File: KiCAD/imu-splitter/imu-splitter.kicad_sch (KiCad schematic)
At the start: 11 parts, among them J1 4P4C, J2 4P4C, J3 4P4C, J4 4P4C, J5 4P4C, J6 4P4C, J7 SHF-113-01-L-D-SM, J8 Conn_01x04, U1 AZ1117-3.3

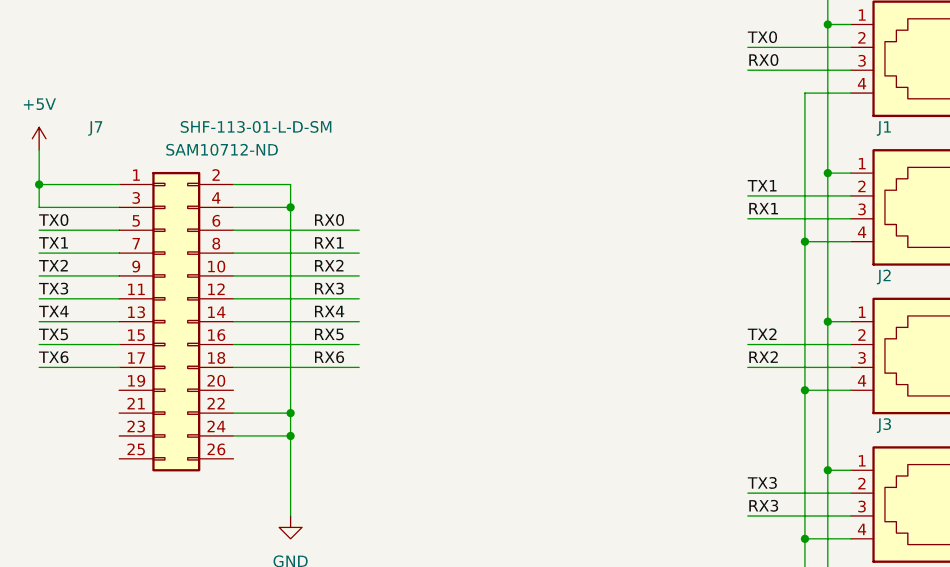
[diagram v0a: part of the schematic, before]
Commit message: tentative placement of splitter
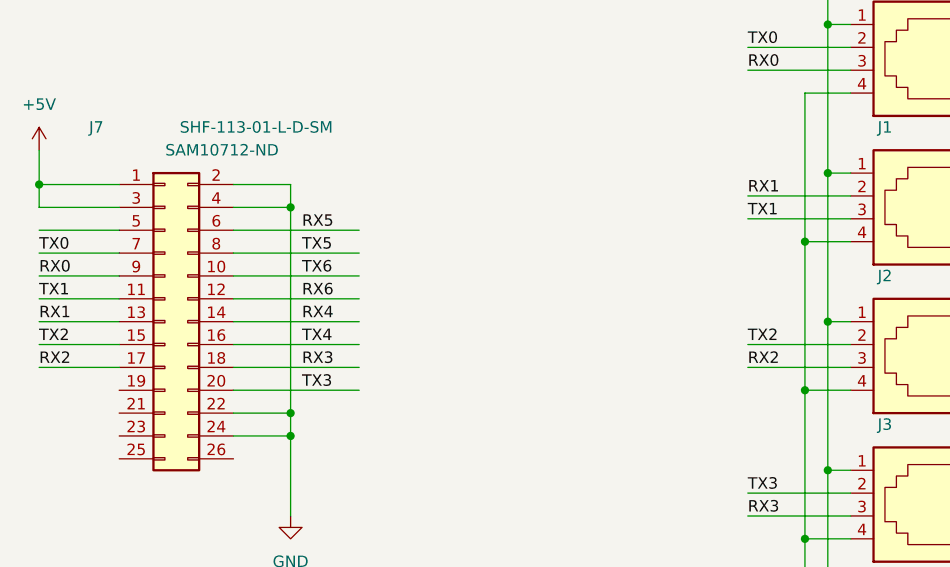
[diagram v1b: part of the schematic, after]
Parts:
- J7: footprint models:SAMTEC_SHF-113-01-L-D-SM -> models:SAMTEC_SHF-113-01-L-D-RA
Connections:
- net RX0: now also J7.9 (Pin_9); no longer J7.6 (Pin_6)
- net RX1: now also J2.2, J7.13 (Pin_13); no longer J2.3, J7.8 (Pin_8)
- net RX2: now also J7.17 (Pin_17); no longer J7.10 (Pin_10)
- net RX3: now also J7.18 (Pin_18); no longer J7.12 (Pin_12)
- net RX5: now also J7.6 (Pin_6); no longer J7.16 (Pin_16)
- net RX6: now also J7.12 (Pin_12); no longer J7.18 (Pin_18)
- net TX0: now also J7.7 (Pin_7); no longer J7.5 (Pin_5)
- net TX1: now also J2.3, J7.11 (Pin_11); no longer J2.2, J7.7 (Pin_7)
- net TX2: now also J7.15 (Pin_15); no longer J7.9 (Pin_9)
- net TX3: now also J7.20 (Pin_20); no longer J7.11 (Pin_11)
- net TX4: now also J7.16 (Pin_16); no longer J7.13 (Pin_13)
- net TX5: now also J7.8 (Pin_8); no longer J7.15 (Pin_15)
- net TX6: now also J7.10 (Pin_10); no longer J7.17 (Pin_17)
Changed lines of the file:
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@@
+    (stroke (width 0) (type default))
+  )
+  (wire (pts (xy 57.15 101.6) (xy 71.12 101.6))
     (stroke (width 0) (type default))
   )
@@
     (stroke (width 0) (type default))
   )
+  (wire (pts (xy 57.15 96.52) (xy 71.12 96.52))
+    (stroke (width 0) (type default))
+  )
   (wire (pts (xy 35.56 96.52) (xy 44.45 96.52))
     (stroke (width 0) (type default))
@@
     (stroke (width 0) (type default))
   )
-  (wire (pts (xy 57.15 96.52) (xy 71.12 96.52))
-    (stroke (width 0) (type default))
-  )
   (wire (pts (xy 57.15 88.9) (xy 71.12 88.9))
     (stroke (width 0) (type default))
@@
     (stroke (width 0) (type default))
   )
-  (label "TX2" (at 35.56 88.9 0) (fields_autoplaced)
+  (label "TX2" (at 35.56 96.52 0) (fields_autoplaced)
     (effects (font (size 1.27 1.27)) (justify left bottom))
   )
@@
     (effects (font (size 1.27 1.27)) (justify left bottom))
   )
-  (label "RX6" (at 66.04 99.06 0) (fields_autoplaced)
-    (effects (font (size 1.27 1.27)) (justify left bottom))
-  )
-  (label "TX1" (at 114.3 80.01 0) (fields_autoplaced)
-    (effects (font (size 1.27 1.27)) (justify left bottom))
-  )
-  (label "TX1" (at 35.56 86.36 0) (fields_autoplaced)
+  (label "TX5" (at 114.3 146.05 0) (fields_autoplaced)
+    (effects (font (size 1.27 1.27)) (justify left bottom))
+  )
+  (label "RX6" (at 64.77 91.44 0) (fields_autoplaced)
+    (effects (font (size 1.27 1.27)) (justify left bottom))
+  )
+  (label "TX1" (at 114.3 82.55 0) (fields_autoplaced)
+    (effects (font (size 1.27 1.27)) (justify left bottom))
+  )
+  (label "TX1" (at 35.56 91.44 0) (fields_autoplaced)
     (effects (font (size 1.27 1.27)) (justify left bottom))
   )
@@
     (effects (font (size 1.27 1.27)) (justify left bottom))
   )
-  (label "TX5" (at 114.3 146.05 0) (fields_autoplaced)
-    (effects (font (size 1.27 1.27)) (justify left bottom))
-  )
-  (label "TX3" (at 35.56 91.44 0) (fields_autoplaced)
-    (effects (font (size 1.27 1.27)) (justify left bottom))
-  )
-  (label "TX4" (at 35.56 93.98 0) (fields_autoplaced)
+  (label "TX5" (at 64.77 86.36 0) (fields_autoplaced)
+    (effects (font (size 1.27 1.27)) (justify left bottom))
+  )
+  (label "TX3" (at 64.77 101.6 0) (fields_autoplaced)
+    (effects (font (size 1.27 1.27)) (justify left bottom))
+  )
+  (label "TX4" (at 64.77 96.52 0) (fields_autoplaced)
     (effects (font (size 1.27 1.27)) (justify left bottom))
   )
@@
     (effects (font (size 1.27 1.27)) (justify left bottom))
   )
-  (label "RX3" (at 66.04 91.44 0) (fields_autoplaced)
-    (effects (font (size 1.27 1.27)) (justify left bottom))
-  )
-  (label "TX0" (at 35.56 83.82 0) (fields_autoplaced)
-    (effects (font (size 1.27 1.27)) (justify left bottom))
-  )
-  (label "RX5" (at 66.04 96.52 0) (fields_autoplaced)
+  (label "RX3" (at 64.77 99.06 0) (fields_autoplaced)
+    (effects (font (size 1.27 1.27)) (justify left bottom))
+  )
+  (label "TX0" (at 35.56 86.36 0) (fields_autoplaced)
+    (effects (font (size 1.27 1.27)) (justify left bottom))
+  )
+  (label "RX5" (at 64.77 83.82 0) (fields_autoplaced)
     (effects (font (size 1.27 1.27)) (justify left bottom))
   )
@@
     (effects (font (size 1.27 1.27)) (justify left bottom))
   )
-  (label "RX0" (at 66.04 83.82 0) (fields_autoplaced)
-    (effects (font (size 1.27 1.27)) (justify left bottom))
-  )
-  (label "RX1" (at 66.04 86.36 0) (fields_autoplaced)
+  (label "RX0" (at 35.56 88.9 0) (fields_autoplaced)
+    (effects (font (size 1.27 1.27)) (justify left bottom))
+  )
+  (label "RX1" (at 35.56 93.98 0) (fields_autoplaced)
     (effects (font (size 1.27 1.27)) (justify left bottom))
   )
@@
     (effects (font (size 1.27 1.27)) (justify left bottom))
   )
-  (label "RX2" (at 66.04 88.9 0) (fields_autoplaced)
+  (label "RX2" (at 35.56 99.06 0) (fields_autoplaced)
     (effects (font (size 1.27 1.27)) (justify left bottom))
   )
@@
     (effects (font (size 1.27 1.27)) (justify left bottom))
   )
-  (label "TX6" (at 35.56 99.06 0) (fields_autoplaced)
-    (effects (font (size 1.27 1.27)) (justify left bottom))
-  )
-  (label "RX1" (at 114.3 82.55 0) (fields_autoplaced)
+  (label "TX6" (at 64.77 88.9 0) (fields_autoplaced)
+    (effects (font (size 1.27 1.27)) (justify left bottom))
+  )
+  (label "RX1" (at 114.3 80.01 0) (fields_autoplaced)
     (effects (font (size 1.27 1.27)) (justify left bottom))
   )
@@
     (effects (font (size 1.27 1.27)) (justify left bottom))
   )
-  (label "TX5" (at 35.56 96.52 0) (fields_autoplaced)
-    (effects (font (size 1.27 1.27)) (justify left bottom))
-  )
-  (label "RX4" (at 66.04 93.98 0) (fields_autoplaced)
+  (label "RX4" (at 64.77 93.98 0) (fields_autoplaced)
     (effects (font (size 1.27 1.27)) (justify left bottom))
   )
@@
       (effects (font (size 1.27 1.27)))
     )
-    (property "Footprint" "models:SAMTEC_SHF-113-01-L-D-SM" (at 49.53 93.98 0)
-      (effects (font (size 1.27 1.27)) hide)
-    )
+    (property "Footprint" "models:SAMTEC_SHF-113-01-L-D-RA" (at 49.53 93.98 0)
+      (effects (font (size 1.27 1.27)) hide)
+    )

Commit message: updates before v1 fab
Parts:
- added D1, D2: LED, LED_SMD:LED_0805_2012Metric_Pad1.15x1.40mm_HandSolder, symbol Device:LED
- added J9: Conn_01x05, Connector_PinHeader_2.54mm:PinHeader_1x05_P2.54mm_Vertical, symbol Connector_Generic:Conn_01x05
- added R1: 1.5k, Resistor_SMD:R_0805_2012Metric_Pad1.20x1.40mm_HandSolder, symbol Device:R_US
- added R2: 510, Capacitor_SMD:C_0805_2012Metric_Pad1.18x1.45mm_HandSolder, symbol Device:R_US
- C1, C2: footprint Capacitor_SMD:C_0805_2012Metric -> Capacitor_SMD:C_0805_2012Metric_Pad1.18x1.45mm_HandSolder
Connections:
- net +3.3V: now also J9.2 (Pin_2), R2.1
- net +5V: now also J9.1 (Pin_1), R1.1
- net GND: now also D1.1 (K), D2.1 (K), J9.5 (Pin_5)
- net RX0: now also J7.14 (Pin_14), J9.4 (Pin_4); no longer J7.9 (Pin_9)
- net RX1: now also J7.12 (Pin_12); no longer J7.13 (Pin_13)
- net RX2: now also J7.6 (Pin_6); no longer J7.17 (Pin_17)
- net RX3: now also J7.9 (Pin_9); no longer J7.18 (Pin_18)
- net RX4: now also J7.17 (Pin_17); no longer J7.14 (Pin_14)
- net RX5: now also J7.21 (Pin_21); no longer J7.6 (Pin_6)
- net RX6: now also J7.11 (Pin_11); no longer J7.12 (Pin_12)
- net TX0: now also J7.16 (Pin_16), J9.3 (Pin_3); no longer J7.7 (Pin_7)
- net TX1: now also J7.10 (Pin_10); no longer J7.11 (Pin_11)
- net TX2: now also J7.8 (Pin_8); no longer J7.15 (Pin_15)
- net TX3: now also J7.7 (Pin_7); no longer J7.20 (Pin_20)
- net TX4: now also J7.15 (Pin_15); no longer J7.16 (Pin_16)
- net TX5: now also J7.19 (Pin_19); no longer J7.8 (Pin_8)
- net TX6: now also J7.13 (Pin_13); no longer J7.10 (Pin_10)
- new net: D1.2 (A), R1.2
- new net: D2.2 (A), R2.2
- no-connect marks 0 -> 3
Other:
- note added: "Test Point"
- moved on the sheet: C2

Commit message: Update KiCAD, start software
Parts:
- C1: CatNo (none) -> 1276-1096-1-ND; MfgNo (none) -> CL21A106KOQNNNE
- C2: CatNo (none) -> 1276-6526-1-ND; MfgNo (none) -> CL21A226KOQNNNE
- D1, D2: CatNo (none) -> 350-5973006607FCT-ND; MfgNo (none) -> 5973006607F
- J1, J2, J3, J4, J5, J6: CatNo (none) -> AE10381-ND; MfgNo (none) -> A-2004-3-4-LP-N-R
- J7: MfgNo (none) -> SHF-113-01-L-D-SM
- J8: CatNo (none) -> SAM10242-ND; MfgNo (none) -> TMS-104-01-G-S
- J9: CatNo (none) -> 609-3462-ND; MfgNo (none) -> 68000-105HLF
- R1: CatNo (none) -> 311-1.50KCRCT-ND; MfgNo (none) -> RC0805FR-071K5L
- R2: CatNo (none) -> 311-510CRCT-ND; MfgNo (none) -> RC0805FR-07510RL
- U1: MfgNo (none) -> AZ1117CH2-3.3TRG1
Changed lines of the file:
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@@
+      (effects (font (size 1.27 1.27)) hide)
+    )
+    (property "CatNo" "AE10381-ND" (at 135.89 80.01 0)
+      (effects (font (size 1.27 1.27)) hide)
+    )
+    (property "MfgNo" "A-2004-3-4-LP-N-R" (at 135.89 80.01 0)
       (effects (font (size 1.27 1.27)) hide)
     )
@@
       (effects (font (size 1.27 1.27)) hide)
     )
+    (property "CatNo" "1276-1096-1-ND" (at 62.23 45.72 0)
+      (effects (font (size 1.27 1.27)) hide)
+    )
+    (property "MfgNo" "CL21A106KOQNNNE" (at 62.23 45.72 0)
+      (effects (font (size 1.27 1.27)) hide)
+    )
     (pin "2")
     (pin "1")
@@
       (effects (font (size 1.27 1.27)) hide)
     )
+    (property "CatNo" "350-5973006607FCT-ND" (at 53.34 49.53 0)
+      (effects (font (size 1.27 1.27)) hide)
+    )
+    (property "MfgNo" "5973006607F" (at 53.34 49.53 0)
+      (effects (font (size 1.27 1.27)) hide)
+    )
     (pin "2")
     (pin "1")
@@
     )
     (property "Datasheet" "~" (at 53.34 39.37 0)
+      (effects (font (size 1.27 1.27)) hide)
+    )
+    (property "MfgNo" "RC0805FR-071K5L" (at 53.34 39.37 0)
+      (effects (font (size 1.27 1.27)) hide)
+    )
+    (property "CatNo" "311-1.50KCRCT-ND" (at 53.34 39.37 0)
       (effects (font (size 1.27 1.27)) hide)
     )
@@
       (effects (font (size 1.27 1.27)) hide)
     )
+    (property "CatNo" "AE10381-ND" (at 135.89 96.52 0)
+      (effects (font (size 1.27 1.27)) hide)
+    )
+    (property "MfgNo" "A-2004-3-4-LP-N-R" (at 135.89 96.52 0)
+      (effects (font (size 1.27 1.27)) hide)
+    )
     (pin "1")
     (pin "2")
@@
     )
     (property "Datasheet" "~" (at 67.31 144.78 0)
+      (effects (font (size 1.27 1.27)) hide)
+    )
+    (property "MfgNo" "68000-105HLF" (at 67.31 144.78 0)
+      (effects (font (size 1.27 1.27)) hide)
+    )
+    (property "CatNo" "609-3462-ND" (at 67.31 144.78 0)
       (effects (font (size 1.27 1.27)) hide)
     )
@@
     (property "CatNo" "SAM10712-ND" (at 55.88 74.93 0)
       (effects (font (size 1.27 1.27)))
+    )
+    (property "MfgNo" "SHF-113-01-L-D-SM" (at 49.53 93.98 0)
+      (effects (font (size 1.27 1.27)) hide)
     )
     (pin "5")
@@
       (effects (font (size 1.27 1.27)) hide)
     )
+    (property "CatNo" "AE10381-ND" (at 135.89 146.05 0)
+      (effects (font (size 1.27 1.27)) hide)
+    )
+    (property "MfgNo" "A-2004-3-4-LP-N-R" (at 135.89 146.05 0)
+      (effects (font (size 1.27 1.27)) hide)
+    )
     (pin "1")
     (pin "2")
@@
       (effects (font (size 1.27 1.27)) hide)
     )
+    (property "MfgNo" "TMS-104-01-G-S" (at 130.81 168.91 0)
+      (effects (font (size 1.27 1.27)) hide)
+    )
+    (property "CatNo" "SAM10242-ND" (at 130.81 168.91 0)
+      (effects (font (size 1.27 1.27)) hide)
+    )
     (pin "4")
     (pin "1")
@@
     )
     (property "Datasheet" "~" (at 86.36 45.72 0)
+      (effects (font (size 1.27 1.27)) hide)
+    )
+    (property "CatNo" "1276-6526-1-ND" (at 86.36 45.72 0)
+      (effects (font (size 1.27 1.27)) hide)
+    )
+    (property "MfgNo" "CL21A226KOQNNNE" (at 86.36 45.72 0)
       (effects (font (size 1.27 1.27)) hide)
     )
@@
       (effects (font (size 1.27 1.27)) hide)
     )
+    (property "CatNo" "AE10381-ND" (at 135.89 63.5 0)
+      (effects (font (size 1.27 1.27)) hide)
+    )
+    (property "MfgNo" "A-2004-3-4-LP-N-R" (at 135.89 63.5 0)
+      (effects (font (size 1.27 1.27)) hide)
+    )
     (pin "1")
     (pin "2")
@@
       (effects (font (size 1.27 1.27)) hide)
     )
+    (property "CatNo" "AE10381-ND" (at 135.89 113.03 0)
+      (effects (font (size 1.27 1.27)) hide)
+    )
+    (property "MfgNo" "A-2004-3-4-LP-N-R" (at 135.89 113.03 0)
+      (effects (font (size 1.27 1.27)) hide)
+    )
     (pin "1")
     (pin "2")
@@
       (effects (font (size 1.27 1.27)) hide)
     )
+    (property "MfgNo" "RC0805FR-07510RL" (at 96.52 39.37 0)
+      (effects (font (size 1.27 1.27)) hide)
+    )
+    (property "CatNo" "311-510CRCT-ND" (at 96.52 39.37 0)
+      (effects (font (size 1.27 1.27)) hide)
+    )
     (pin "2")
     (pin "1")
@@
     )
     (property "Datasheet" "~" (at 96.52 49.53 0)
+      (effects (font (size 1.27 1.27)) hide)
+    )
+    (property "CatNo" "350-5973006607FCT-ND" (at 96.52 49.53 0)
+      (effects (font (size 1.27 1.27)) hide)
+    )
+    (property "MfgNo" "5973006607F" (at 96.52 49.53 0)
       (effects (font (size 1.27 1.27)) hide)
     )
@@
       (effects (font (size 1.27 1.27)))
     )
+    (property "MfgNo" "AZ1117CH2-3.3TRG1" (at 77.47 35.56 0)
+      (effects (font (size 1.27 1.27)) hide)
+    )
     (pin "2")
     (pin "1")
@@
       (effects (font (size 1.27 1.27)) hide)
     )
+    (property "CatNo" "AE10381-ND" (at 135.89 129.54 0)
+      (effects (font (size 1.27 1.27)) hide)
+    )
+    (property "MfgNo" "A-2004-3-4-LP-N-R" (at 135.89 129.54 0)
+      (effects (font (size 1.27 1.27)) hide)
+    )

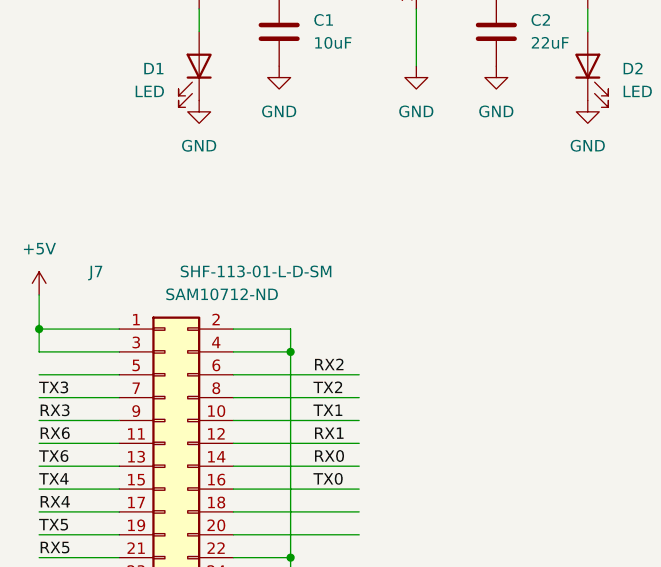
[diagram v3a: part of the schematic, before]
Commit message: KiCAD 8: Update schem P/N on 26 pin header to RA
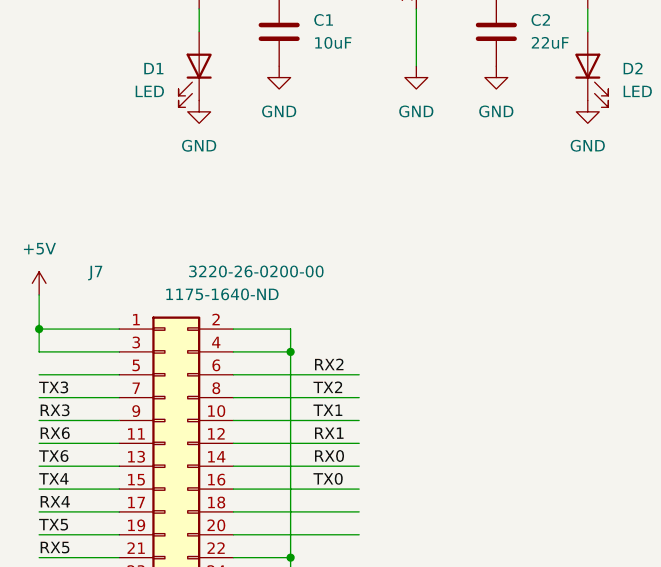
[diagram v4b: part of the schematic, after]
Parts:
- J7: value SHF-113-01-L-D-SM -> 3220-26-0200-00; CatNo SAM10712-ND -> 1175-1640-ND; MfgNo SHF-113-01-L-D-SM -> 3220-26-0200-00
